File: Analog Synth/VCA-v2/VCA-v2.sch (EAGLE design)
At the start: 47 parts, among them IC1 79L05, IC2 TL084P, IC3 TL084P, IC4 CA3046

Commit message: same;tbh;smh fam
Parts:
- removed IC3: TL084P, linear:TL084P
- removed IC4: CA3046, !synthdiy:CA3046
- renumbered CV-A to CV
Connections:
- removed net N$19: IC2D.+IN, R-AUDIO-IN.S
- removed net N$25: C8.1, IC3B.-IN, R-BALANCE.S
- removed net N$3: CV.P2, IC2A.+IN
- removed net N$5: R-BALANCE.E, R2.2
- removed net N$7: R-BALANCE.A, R3.1
- removed net N$9: AUDIO-IN.P2, R-AUDIO-IN.E
- net +12V: no longer IC3P.V+
- net -12V: no longer IC3P.V-, IC4T5.E
- net GND: no longer IC3A.+IN, IC3B.+IN, IC3D.+IN, IC4T1-T2.E, R-AUDIO-IN.A
- net N$15: no longer IC3A.OUT
- net N$2: no longer IC4T1-T2.B2
- net N$20: no longer IC3D.-IN
- net N$21: no longer IC4T1-T2.B1
- net N$23: no longer C8.2, IC3B.OUT, R3.2
- net N$24: no longer IC4T1-T2.C2
- net N$26: no longer IC4T1-T2.C1
- net N$28: no longer IC3C.+IN
- net N$30: no longer IC3C.-IN
- net N$31: no longer IC3C.OUT
- net N$34: no longer IC3D.OUT
- net N$6: no longer IC3A.-IN
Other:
- moved on the sheet: AUDIO-IN, R-AUDIO-IN

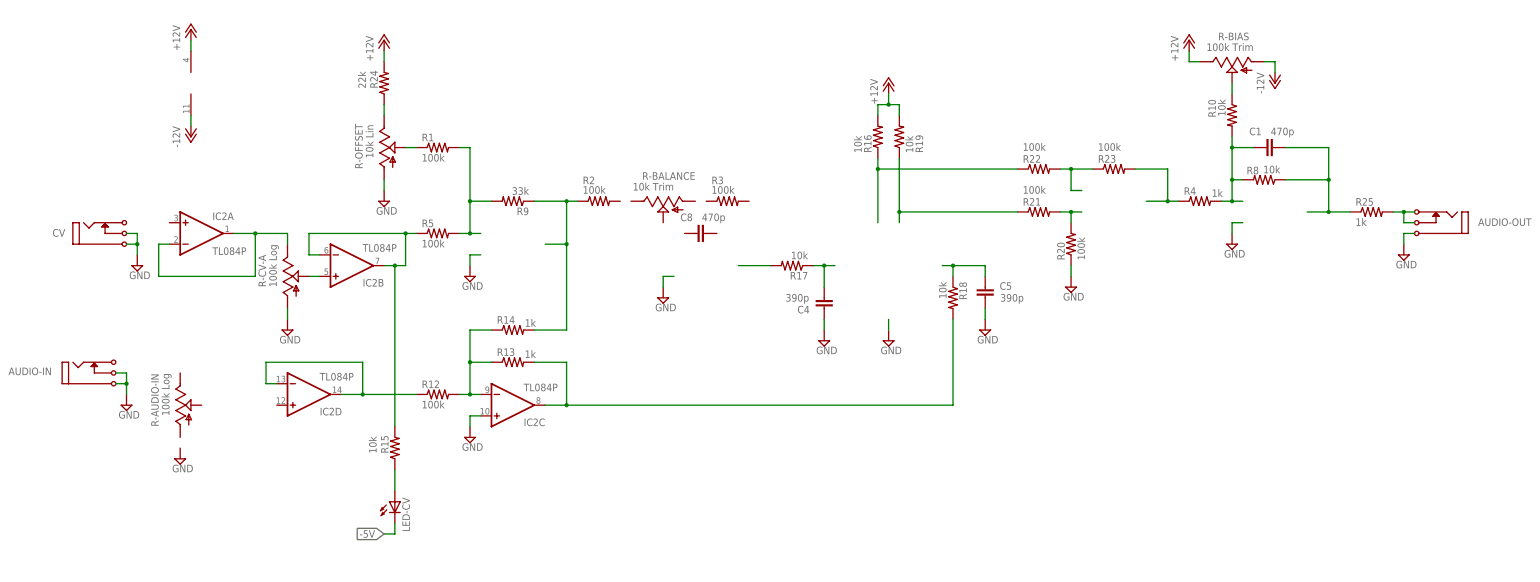
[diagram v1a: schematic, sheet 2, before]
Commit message: created VCA-v2 schematic. PCB exists, but it is not layed out or routed
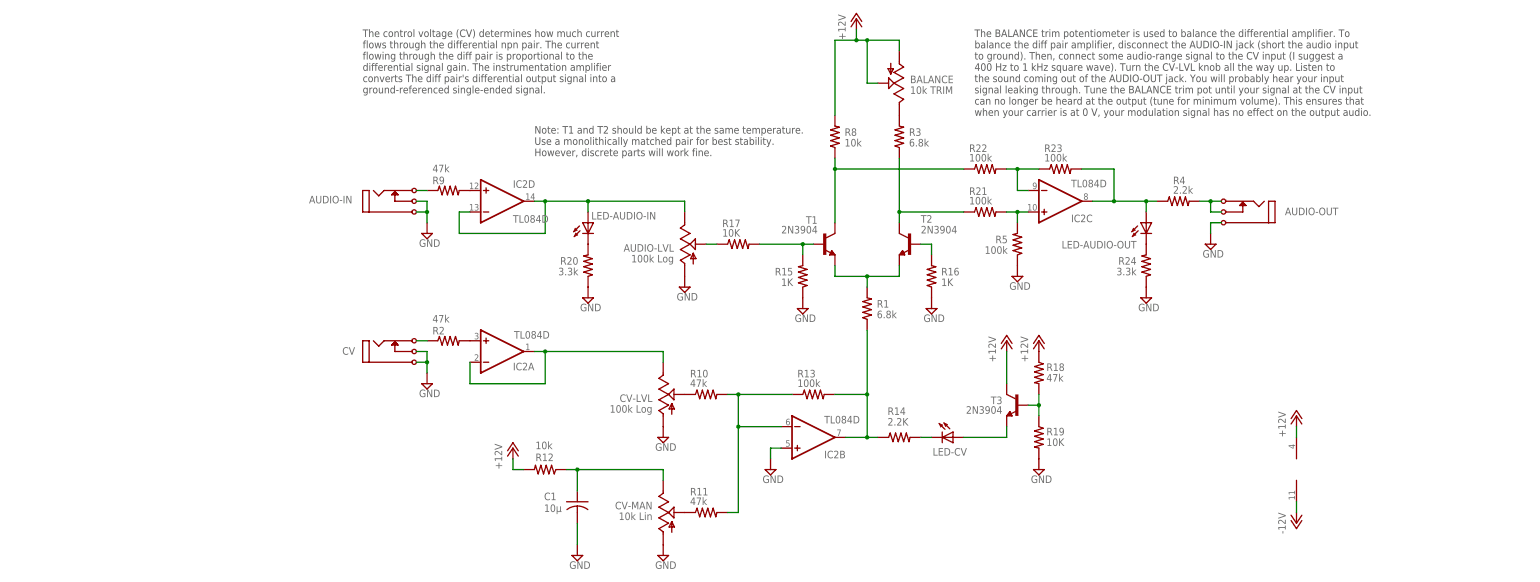
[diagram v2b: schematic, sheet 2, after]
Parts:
- removed C10: 10µ, rcl:C-US025-050X050
- removed C4, C5: 390p, capacitor-wima:C2.5/2
- removed C8: 470p, capacitor-wima:C2.5/2
- removed IC1: 79L05, linear:79L05Z
- removed R-AUDIO-IN, R-CV-A: 100k Log, pot:TRIM_US-B64Y
- removed R-BALANCE: 10k Trim, pot:TRIM_US-B64Y
- removed R-BIAS: 100k Trim, pot:TRIM_US-B64Y
- removed R-OFFSET: 10k Lin, pot:TRIM_US-B64Y
- removed R25: 1k, resistor:R-US_0204/7
- added AUDIO-LVL, CV-LVL: 100k Log, pot:TRIM_US-B64Y
- added BALANCE: 10k TRIM, pot:TRIM_US-B64Y
- added CV-MAN: 10k Lin, pot:TRIM_US-B64Y
- added LED-AUDIO-IN, LED-AUDIO-OUT: TLLG4400, led:TLLG4400
- added R11: 47k, resistor:R-US_R0603
- added T1, T2, T3: 2N3904, transistor-neu-to92:2N3904
- C1: value 470p -> 10µ; device capacitor-wima:C2.5/2 -> rcl:C-US025-050X050
- IC2: value TL084P -> TL084D; device linear:TL084P -> linear:TL084D
- R1, R3: value 100k -> 6.8k; device resistor:R-US_0204/2V -> resistor:R-US_R0603
- R10: value 10k -> 47k; device resistor:R-US_0204/2V -> resistor:R-US_R0603
- R12: value 100k -> 10k; device resistor:R-US_0204/2V -> resistor:R-US_R0603
- R13: value 1k -> 100k; device resistor:R-US_0204/2V -> resistor:R-US_R0603
- R14: value 1k -> 2.2K; device resistor:R-US_0204/2V -> resistor:R-US_R0603
- R15, R16: value 10k -> 1K; device resistor:R-US_0204/2V -> resistor:R-US_R0603
- R17, R19: value 10k -> 10K; device resistor:R-US_0204/2V -> resistor:R-US_R0603
- R18: value 10k -> 47k; device resistor:R-US_0204/7 -> resistor:R-US_R0603
- R2: value 100k -> 47k; device resistor:R-US_0204/2V -> resistor:R-US_R0603
- R20: value 100k -> 3.3k; device resistor:R-US_0204/2V -> resistor:R-US_R0603
- R21, R22, R23, R5, R8: device resistor:R-US_0204/2V -> resistor:R-US_R0603
- R24: value 22k -> 3.3k; device resistor:R-US_0204/2V -> resistor:R-US_R0603
- R4: value 1k -> 2.2k; device resistor:R-US_0204/2V -> resistor:R-US_R0603
- R6, R7: device resistor:R-US_0204/7 -> resistor:R-US_R0603
- R9: value 33k -> 47k; device resistor:R-US_0204/2V -> resistor:R-US_R0603
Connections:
- removed net -5V: C10.2, IC1.VO, LED-CV.C
- removed net N$22: IC2C.-IN, R12.2, R13.1, R14.1
- removed net N$27: IC2C.OUT, R13.2, R18.2
- removed net N$34: C1.2, R25.1, R8.1
- removed net N$49: R-OFFSET.E, R24.1
- new net LED_SUPPLY: LED-CV.A, T3.E
- new net N$16: R15.2, R17.2, T1.B
- new net N$17: IC2B.-IN, R10.2, R11.2, R13.1
- new net N$19: R16.2, T2.B
- new net N$3: IC2A.+IN, R2.2
- new net N$5: CV.P2, R2.1
- new net N$7: IC2D.+IN, R9.2
- new net N$9: AUDIO-LVL.E, IC2D.-IN, IC2D.OUT, LED-AUDIO-IN.A
- net +12V: now also BALANCE.A, BALANCE.S, R12.2, R18.1, R8.2, T3.C; no longer R-BIAS.E, R16.2, R19.2, R24.2
- net -12V: no longer IC1.VI, R-BIAS.A
- net GND: now also AUDIO-LVL.A, C1.2, CV-LVL.A, CV-MAN.A, IC2B.+IN, R15.1, R16.1, R19.2, R24.1, R5.1; no longer C10.1, C4.1, C5.2, IC1.GND, IC2C.+IN, R-CV-A.A, R-OFFSET.A
- net N$1: now also R1.1, R13.2, R14.1; no longer IC2B.-IN, R15.2, R5.1
- net N$11: now also CV-LVL.S; no longer R-BIAS.S
- net N$12: now also LED-CV.C, R14.2; no longer LED-CV.A, R15.1
- net N$13: now also CV-MAN.S, R11.1; no longer R-OFFSET.S, R1.1
- net N$14: now also C1.1, CV-MAN.E, R12.1; no longer IC2B.+IN, R-CV-A.S
- net N$15: now also R1.2, T1.E, T2.E; no longer R14.2, R2.1, R9.1
- net N$18: now also AUDIO-LVL.S, R17.1; no longer IC2D.-IN, IC2D.OUT, R12.1
- net N$2: now also BALANCE.E, R3.2; no longer C4.2, R17.1
- net N$20: now also R18.2, R19.1, T3.B; no longer C1.1, R10.2, R4.2, R8.2
- net N$21: now also LED-AUDIO-IN.C, R20.2; no longer C5.1, R18.1
- net N$23: now also LED-AUDIO-OUT.C, R24.2; no longer R17.2
- net N$24: now also R8.1, T1.C; no longer R16.1
- net N$26: now also R3.1, T2.C; no longer R19.1
- net N$28: now also IC2C.+IN, R5.2; no longer R20.2
- net N$30: now also IC2C.-IN
- net N$31: now also IC2C.OUT, LED-AUDIO-OUT.A
- net N$32: now also R4.2; no longer R25.2
- net N$4: now also CV-LVL.E; no longer R-CV-A.E
- net N$6: now also AUDIO-IN.P2, R9.1; no longer R1.2, R5.2, R9.2
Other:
- note added: "2016-June"
- note added: "A simple linear-envelope VCA"
- note added: "Note: T1 and T2 should be kept at the same temperature. Use a monolithically matched pair for best stability. However, discrete parts will work fine."
- note added: "Ryan Jensen"
- note added: "The BALANCE trim potentiometer is used to balance the differential amplifier. To balance the diff pair amplifier, disconnect the AUDIO-IN jack (short the audio input to ground). Then, connect some audio-range signal to the CV input (I suggest a 400 Hz to 1 kHz square wave). Turn the CV-LVL knob all the way up. Listen to the sound coming out of the AUDIO-OUT jack. You will probably hear your input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"
- note added: "The control voltage (CV) determines how much current flows through the differential npn pair. The current flowing through the diff pair is proportional to the differential signal gain. The instrumentation amplifier converts The diff pair's differential output signal into a ground-referenced single-ended signal."
- note added: "VCA-v2 Voltage Controlled Amplifier"
- moved on the sheet: AUDIO-IN, AUDIO-OUT, C1, C2, C3, C6, C7, CV, IC2A, IC2B, IC2C, IC2D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

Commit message: added DMMT3904W to part library in synth_sch; making progress on VCA-v2 layout
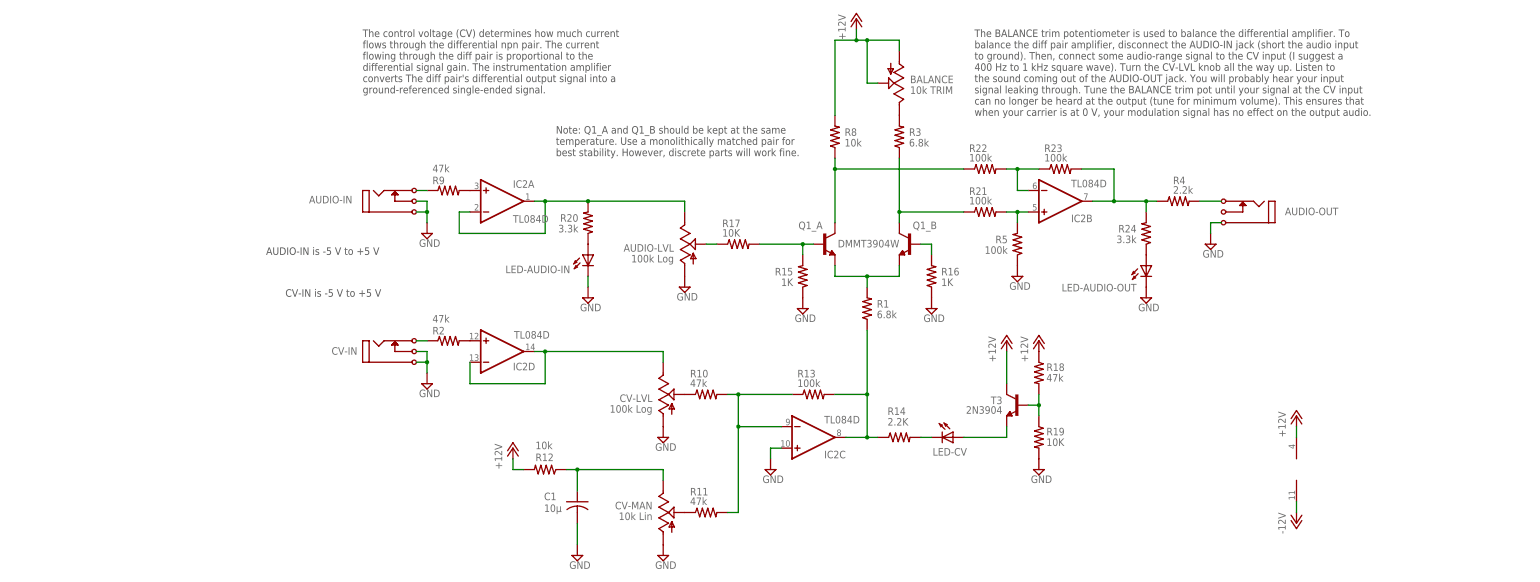
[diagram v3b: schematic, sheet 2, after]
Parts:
- removed T1, T2: 2N3904, transistor-neu-to92:2N3904
- added Q1_: DMMT3904W, !synth_sch:DMMT3904W
- renumbered CV to CV-IN
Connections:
- removed net N$23: LED-AUDIO-OUT.C, R24.2
- new net N$22: LED-AUDIO-OUT.A, R24.1
- net GND: now also IC2C.+IN, LED-AUDIO-IN.C, LED-AUDIO-OUT.C; no longer IC2B.+IN, R20.1, R24.1
- net N$1: now also IC2C.OUT; no longer IC2B.OUT
- net N$15: now also Q1_A.E, Q1_B.E; no longer T1.E, T2.E
- net N$16: now also Q1_A.B; no longer T1.B
- net N$17: now also IC2C.-IN; no longer IC2B.-IN
- net N$19: now also Q1_B.B; no longer T2.B
- net N$21: now also LED-AUDIO-IN.A, R20.1; no longer LED-AUDIO-IN.C, R20.2
- net N$24: now also Q1_A.C; no longer T1.C
- net N$26: now also Q1_B.C; no longer T2.C
- net N$28: now also IC2B.+IN; no longer IC2C.+IN
- net N$3: now also IC2D.+IN; no longer IC2A.+IN
- net N$30: now also IC2B.-IN; no longer IC2C.-IN
- net N$31: now also IC2B.OUT, R24.2; no longer IC2C.OUT, LED-AUDIO-OUT.A
- net N$32: no longer AUDIO-OUT.P3
- net N$4: now also IC2D.-IN, IC2D.OUT; no longer IC2A.-IN, IC2A.OUT
- net N$7: now also IC2A.+IN; no longer IC2D.+IN
- net N$9: now also IC2A.-IN, IC2A.OUT, R20.2; no longer IC2D.-IN, IC2D.OUT, LED-AUDIO-IN.A
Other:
- note added: "AUDIO-IN is -5 V to +5 V"
- note added: "CV-IN is -5 V to +5 V"
- note added: "Note: Q1_A and Q1_B should be kept at the same temperature. Use a monolithically matched pair for best stability. However, discrete parts will work fine."
- note removed: "Note: T1 and T2 should be kept at the same temperature. Use a monolithically matched pair for best stability. However, discrete parts will work fine."
- moved on the sheet: IC2A, IC2B, IC2C, IC2D, LED-AUDIO-IN, LED-AUDIO-OUT, R20, R24
